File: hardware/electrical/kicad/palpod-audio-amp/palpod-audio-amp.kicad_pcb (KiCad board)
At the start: 6 copper layers, 250 x 200 mm, 0 parts

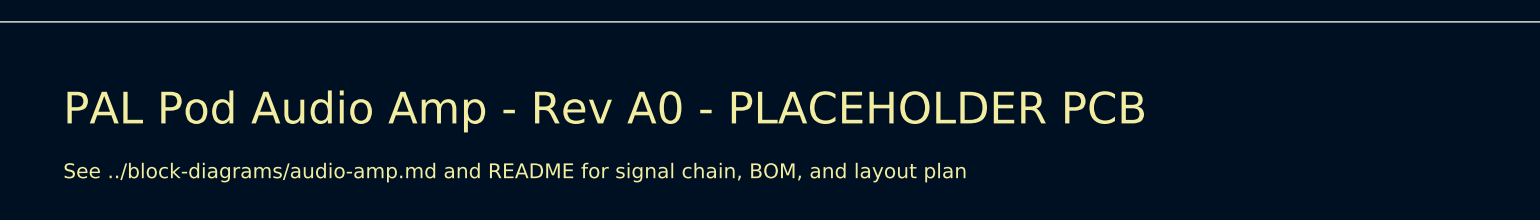
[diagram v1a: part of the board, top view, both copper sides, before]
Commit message: brand: broad KiCad sweep — remaining PAL Pod strings → Hearth
Targeted-pattern sed in ff14a48 missed variants. Broad find-replace
on .kicad_sch/pcb/pro/sym/mod + fp-lib-table + sym-lib-table +
per-project README.md (only where PAL Pod string actually appeared).
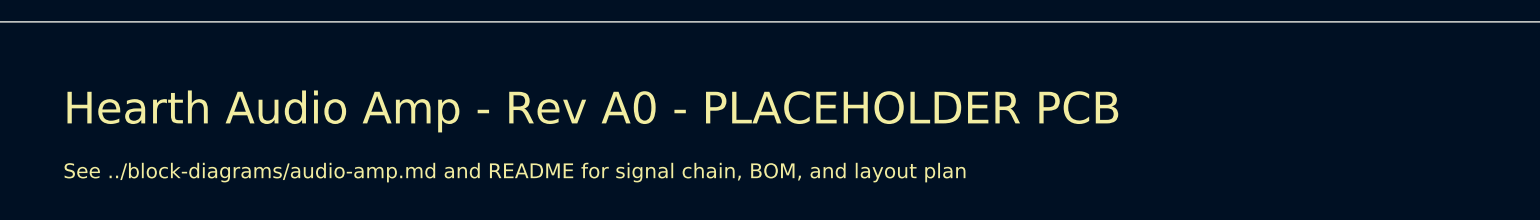
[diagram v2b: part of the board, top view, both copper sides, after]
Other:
- board text added: "Hearth Audio Amp - Rev A0 - PLACEHOLDER PCB"
- board text removed: "PAL Pod Audio Amp - Rev A0 - PLACEHOLDER PCB"
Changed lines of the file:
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@@
   (paper "A3")
   (title_block
-    (title "PAL Pod Audio Amp - PCB")
+    (title "Hearth Audio Amp - PCB")
     (date "2026-08-03")
     (rev "A0")
@@
   (gr_line (start 250 200) (end 0 200)   (stroke (width 0.15) (type solid)) (layer "Edge.Cuts"))
   (gr_line (start 0 200)   (end 0 0)     (stroke (width 0.15) (type solid)) (layer "Edge.Cuts"))
-  (gr_text "PAL Pod Audio Amp - Rev A0 - PLACEHOLDER PCB"
+  (gr_text "Hearth Audio Amp - Rev A0 - PLACEHOLDER PCB"
     (at 10 10 0)
     (layer "F.SilkS")
